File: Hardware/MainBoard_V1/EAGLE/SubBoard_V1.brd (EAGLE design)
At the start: 30 x 50 mm, 17 parts, among them J1 1X2-3.5MM, U1 MAX31855K

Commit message: Layout optimization
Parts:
- moved J4 8.00 mm to (20.0, 6.00)
- moved J5 8.00 mm to (20.0, 14.0)
- moved J6 8.00 mm to (20.0, 24.0)
- moved J8 8.00 mm to (20.0, 35.0)
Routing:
- net D8: track 9.89 -> 17.9 mm
- net A0: track 13.6 -> 5.55 mm
- net A7: track 15.4 -> 10.0 mm
- net A3: track 15.8 -> 10.7 mm
- net A6: track 15.6 -> 10.6 mm
- net A2: track 16.1 -> 11.8 mm
- net A1: track 16.3 -> 12.8 mm
- net 5V: track 64.7 -> 66.1 mm

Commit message: SubBoard exports
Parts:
- added C2: 10uF, rcl:C0805
- added D1, D2: (no value), adafruit:SOD-523
- added R1, R2: 10k, rcl:R0402
- C1: value (none) -> 0.01uF
- J5: device SparkFun-Connectors:JST-2-PTH-NS -> SparkFun-Connectors:JST-2-PTH
- moved J7 8.06 mm to (28.0, 43.0), turned to 180 degrees
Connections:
- new net N$4: D1.A, R1.1, U1.5
- new net N$6: D2.A, R2.1, U1.6
- net 3V3: now also C2.1, R1.2, R2.2, U1.4
- net 5V: no longer U1.4
- net D5: now also D2.K; no longer U1.6
- net D6: now also D1.K; no longer U1.5
- net GND: now also C2.2
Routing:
- net 3V3: track 0.00 -> 62.1 mm, vias 0 -> 2
- net N$4: track 0.00 -> 35.2 mm
- net D6: track 34.5 -> 2.04 mm
- net N$6: track 0.00 -> 31.8 mm
- net D5: track 33.7 -> 2.28 mm
- net D1: track 25.2 -> 21.9 mm
- net 5V: track 66.1 -> 63.1 mm, vias 1 -> 0
- net D0: track 24.2 -> 25.5 mm
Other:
- outline, holes or cut-outs redrawn
- board text added: "+ T R G"
- board text removed: "G R T +"

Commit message: Switch pullups added
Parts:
- added R3, R4: 10K, rcl:R0402
- R1, R2: value 10k -> 10K
- moved J7 3.00 mm to (28.0, 46.0)
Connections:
- net 5V: now also R3.2, R4.2
- net A6: now also R3.1
- net A7: now also R4.1
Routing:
- net 5V: track 63.1 -> 73.4 mm
- net D1: track 21.9 -> 24.1 mm
- net A6: track 10.6 -> 12.4 mm
- net A7: track 10.0 -> 11.9 mm
- net D0: track 25.5 -> 27.0 mm

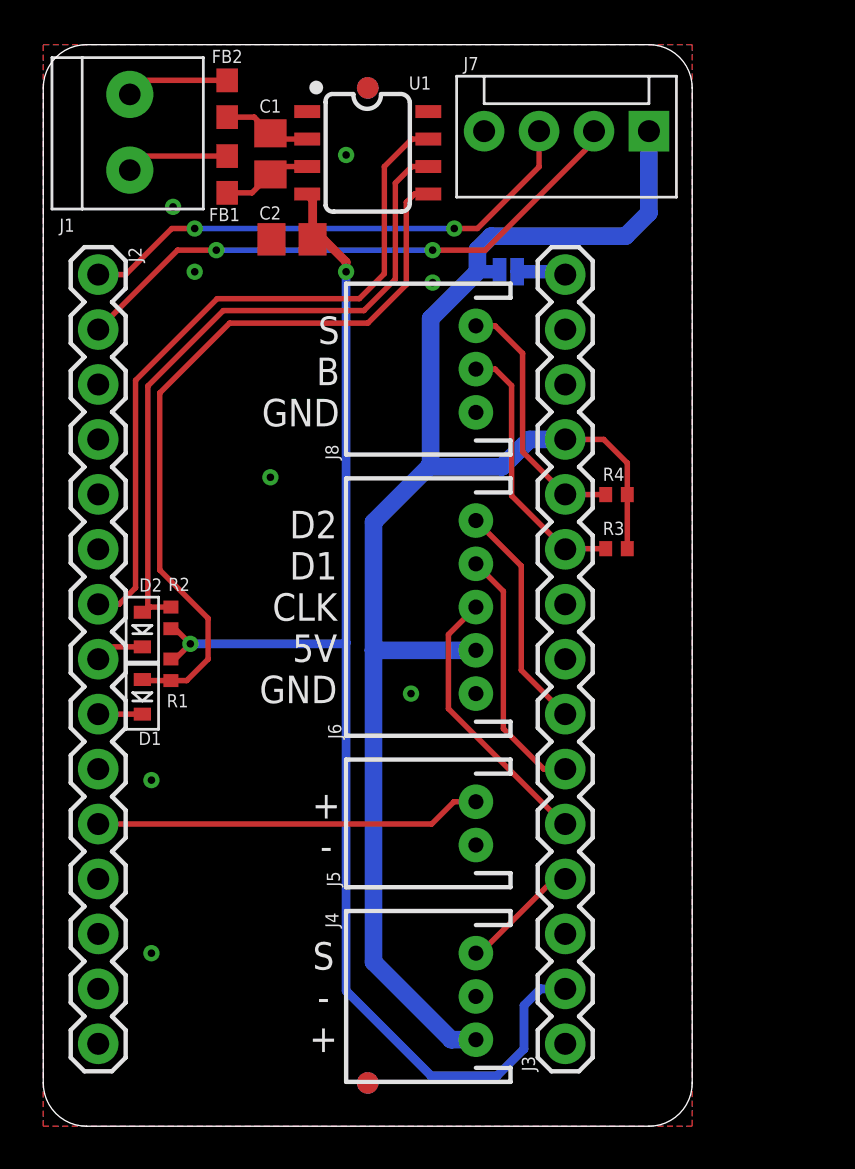
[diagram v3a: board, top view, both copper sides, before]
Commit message: Layout change
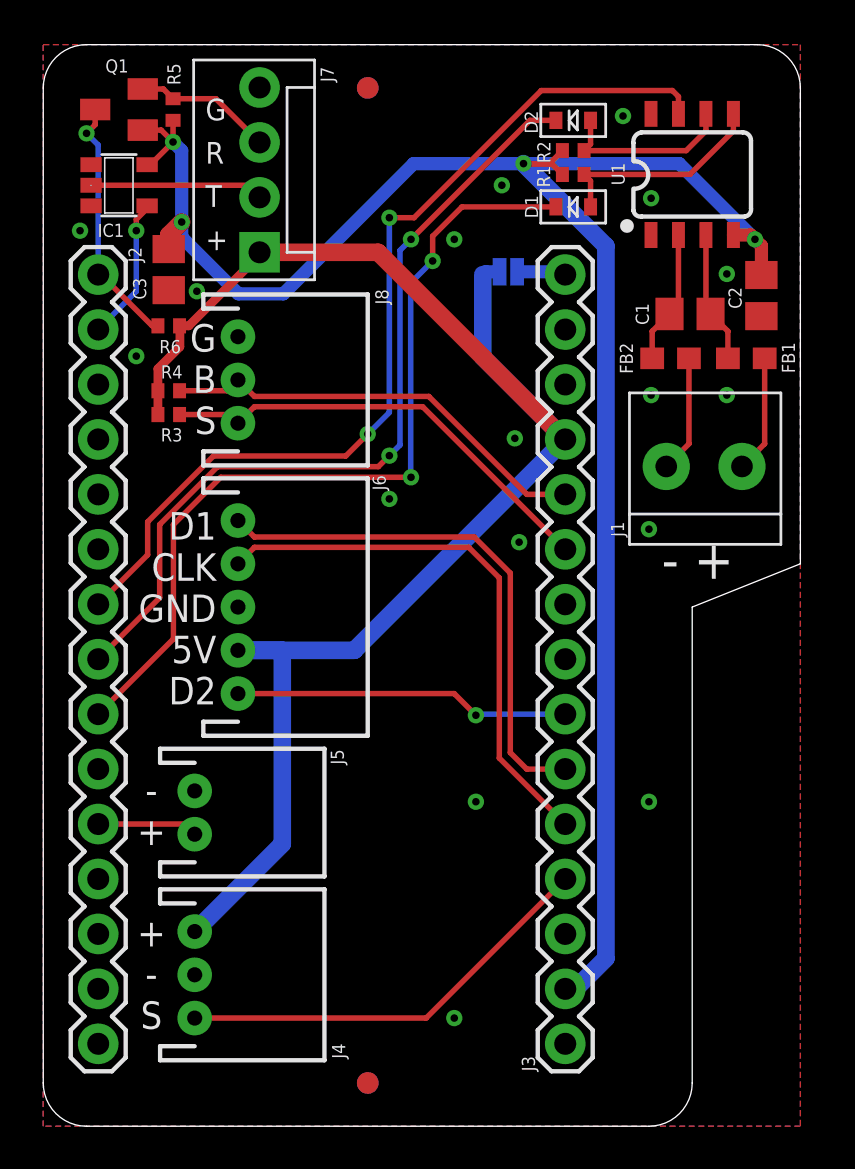
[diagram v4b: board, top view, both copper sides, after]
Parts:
- added C3: 10uF, rcl:C0805
- added IC1: (no value), 74xx-little-de:SOT23-5
- added Q1: (no value), adafruit:SOT23
- added R5, R6: 10K, rcl:R0402
- moved D2 30.8 mm to (24.5, 46.5), turned to 90 degrees
- moved J1 30.7 mm to (30.5, 30.5), turned to 0 degrees
- moved D1 30.2 mm to (24.5, 42.5), turned to 90 degrees
- moved R1 29.5 mm to (24.5, 44.0), turned to 180 degrees
- moved R2 28.5 mm to (24.5, 45.1), turned to 180 degrees
- moved FB1 25.5 mm to (32.5, 35.5), turned to 180 degrees
- moved FB2 23.8 mm to (29.0, 35.5), turned to 180 degrees
- moved C2 21.9 mm to (33.2, 38.4), turned to 270 degrees
- moved R3 21.6 mm to (5.80, 32.9), turned to 180 degrees
- moved R4 21.2 mm to (5.80, 34.0), turned to 180 degrees
- moved C1 20.8 mm to (29.9, 37.5), turned to 0 degrees
- moved J7 18.9 mm to (10.0, 40.4), turned to 90 degrees
- moved U1 15.0 mm to (30.0, 44.0), turned to 0 degrees
- moved J4 13.0 mm to (7.00, 7.00), turned to 270 degrees
- moved J5 13.0 mm to (7.00, 14.5), turned to 270 degrees
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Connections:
- new net RX: J7.3, Q1.2, R5.1
- new net TX: IC1.2, J7.2
- net 3V3: now also C3.1, IC1.5, Q1.1, R5.2
- net 5V: now also J6.4, R6.2; no longer J6.2
- net A1: now also J6.2; no longer J6.3
- net A2: now also J6.1; no longer J6.4
- net A6: now also J8.3; no longer J8.2
- net A7: now also J8.2; no longer J8.3
- net D0: now also IC1.4; no longer J7.2
- net D1: now also Q1.3, R6.1; no longer J7.3
- net GND: now also C3.2, IC1.3, J6.3; no longer J6.1
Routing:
- net D6: track 2.04 -> 39.9 mm, vias 0 -> 2
- net D5: track 2.28 -> 38.7 mm, vias 0 -> 2
- net 3V3: track 62.1 -> 89.5 mm, vias 2 -> 4
- net N$4: track 35.2 -> 10.2 mm
- net N$6: track 31.8 -> 8.32 mm
- net D0: track 27.0 -> 6.66 mm, vias 2 -> 1
- net A0: track 5.55 -> 19.8 mm
- net D8: track 17.9 -> 4.65 mm
- net A2: track 11.8 -> 24.8 mm
- net A1: track 12.8 -> 25.6 mm
- net D1: track 24.1 -> 11.8 mm, vias 2 -> 1
- net D4: track 32.7 -> 43.7 mm, vias 0 -> 2
- net A6: track 12.4 -> 21.0 mm
- net A7: track 11.9 -> 20.2 mm
- net TX: track 0.00 -> 8.02 mm
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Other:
- board size 30 x 50 mm -> 35 x 50 mm
- board text added: "+ - S"
- board text added: "- +"
- board text added: "D1 CLK GND 5V D2"
- board text added: "G B S"
- board text added: "G R T +"
- board text removed: "+ -"
- board text removed: "+ T R G"
- board text removed: "D2 D1 CLK 5V GND"
- board text removed: "S - +"
- board text removed: "S B GND"
- board text removed: "T- T+"

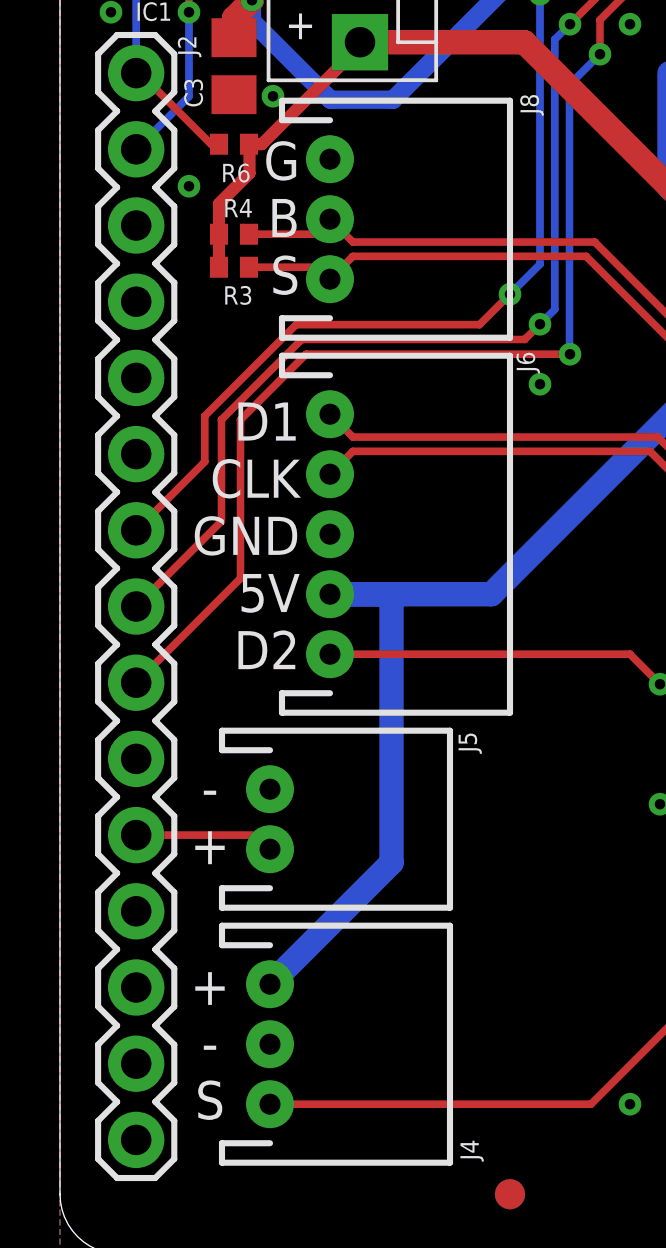
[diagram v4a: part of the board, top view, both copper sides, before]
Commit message: Boiler SSR pin relocation
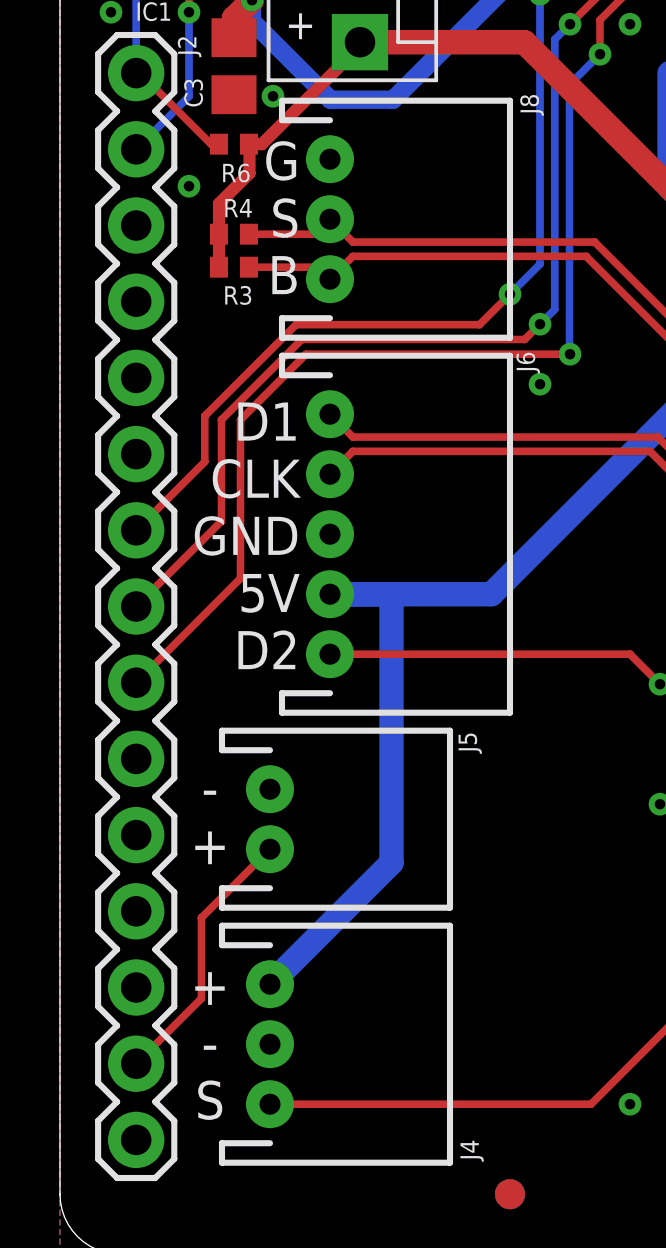
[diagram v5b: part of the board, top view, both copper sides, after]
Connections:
- net D11: now also J5.2
- net D8: no longer J5.2
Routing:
- net D11: track 0.00 -> 9.00 mm
- net D8: track 4.65 -> 0.00 mm
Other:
- board text added: "G S B"
- board text removed: "G B S"
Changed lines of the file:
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@@
 <drawing>
 <settings>
-<setting alwaysvectorfont="yes"/>
+<setting alwaysvectorfont="no"/>
 <setting verticaltext="up"/>
 </settings>
-<grid distance="1" unitdist="mm" unit="mm" style="lines" multiple="1" display="no" altdistance="0.1" altunitdist="mm" altunit="mm"/>
+<grid distance="50" unitdist="mil" unit="mil" style="lines" multiple="1" display="no" altdistance="5" altunitdist="mil" altunit="mil"/>
 <layers>
 <layer number="1" name="Top" color="4" fill="1" visible="yes" active="yes"/>
@@
 <text x="26.714" y="1.534" size="1.778" layer="26" rot="MR90">Gaggiuino</text>
 <text x="8" y="32" size="1.27" layer="25" align="bottom-right">G
-B
-S</text>
+S
+B</text>
 <text x="8" y="19.5" size="1.27" layer="25" align="bottom-right">D1
 CLK
@@
 <signal name="D11">
 <contactref element="J2" pad="14"/>
+<contactref element="J5" pad="2"/>
+<wire x1="2.54" y1="6.35" x2="4.714" y2="8.524" width="0.254" layer="1"/>
+<wire x1="4.714" y1="11.214" x2="7" y2="13.5" width="0.254" layer="1"/>
+<wire x1="4.714" y1="11.214" x2="4.714" y2="8.524" width="0.254" layer="1"/>
 </signal>
 <signal name="D10">
@@
 <signal name="D8">
 <contactref element="J2" pad="11"/>
-<contactref element="J5" pad="2"/>
-<wire x1="7" y1="13.5" x2="6.53" y2="13.97" width="0.254" layer="1"/>
-<wire x1="6.53" y1="13.97" x2="2.54" y2="13.97" width="0.254" layer="1"/>
 </signal>
 <signal name="D7">

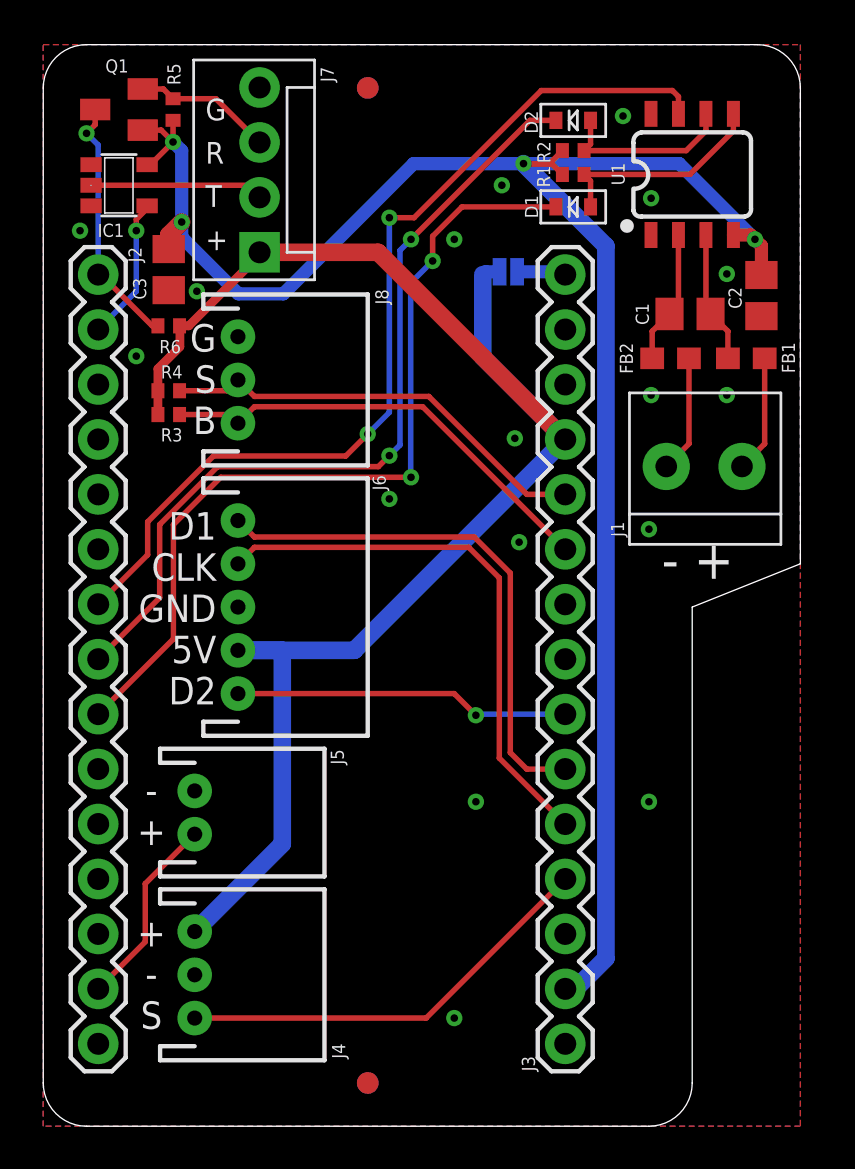
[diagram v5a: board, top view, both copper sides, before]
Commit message: Nextion full buffer IO
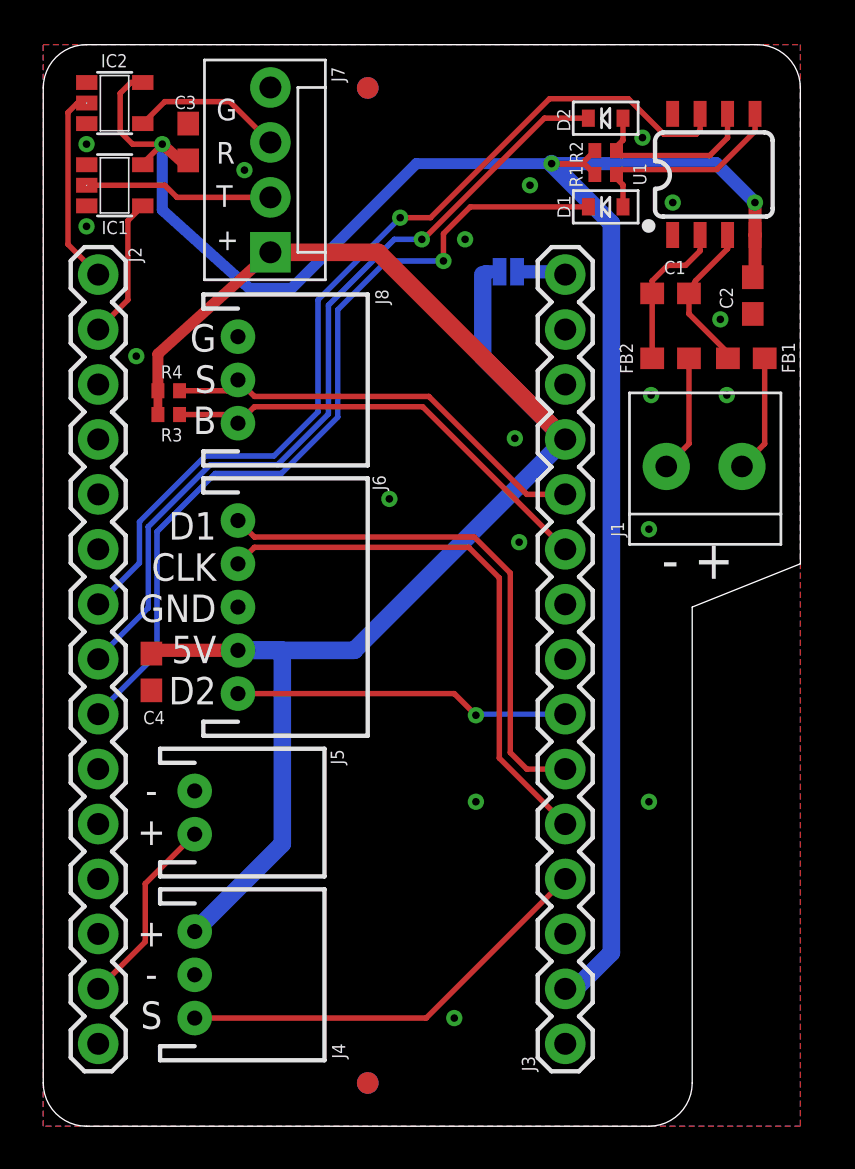
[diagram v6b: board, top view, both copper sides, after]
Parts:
- removed Q1: (no value), adafruit:SOT23
- removed R5, R6: 10K, rcl:R0402
- added C4: 10uF, rcl:C0603
- added IC2: (no value), 74xx-little-de:SOT23-5
- C1, C2, C3: device rcl:C0805 -> rcl:C0603
- moved C3 5.97 mm to (6.70, 45.5), turned to 90 degrees
- moved D2 1.50 mm to (26.0, 46.6)
- moved D1 1.50 mm to (26.0, 42.5)
- moved R1 1.50 mm to (26.0, 44.0)
- moved R2 1.50 mm to (26.0, 45.1)
- moved C1 1.31 mm to (29.0, 38.5)
- moved U1 1.00 mm to (31.0, 44.0)
- moved J7 0.50 mm to (10.5, 40.4)
- moved C2 0.40 mm to (32.8, 38.4)
- moved IC1 0.20 mm to (3.30, 43.5)
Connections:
- net 3V3: now also IC2.5; no longer Q1.1, R5.2
- net 5V: now also C4.1; no longer R6.2
- net D1: now also IC2.2; no longer Q1.3, R6.1
- net GND: now also C4.2, IC2.3
- net RX: now also IC2.4; no longer Q1.2, R5.1
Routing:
- net 5V: track 73.3 -> 77.0 mm
- net D1: track 11.8 -> 9.12 mm, vias 1 -> 0
- net 3V3: track 89.5 -> 91.5 mm, vias 4 -> 3
- net N$5: track 6.12 -> 7.13 mm
- net N$3: track 6.20 -> 7.10 mm
- net TX: track 8.02 -> 8.72 mm
- net RX: track 6.42 -> 7.11 mm
- net D4: track 43.7 -> 43.2 mm, vias 2 -> 1
- net D6: track 39.9 -> 39.4 mm, vias 2 -> 1
- net D5: track 38.7 -> 38.2 mm, vias 2 -> 1
- net D0: track 6.66 -> 6.57 mm, vias 1 -> 0

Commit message: Connector spacing fixed
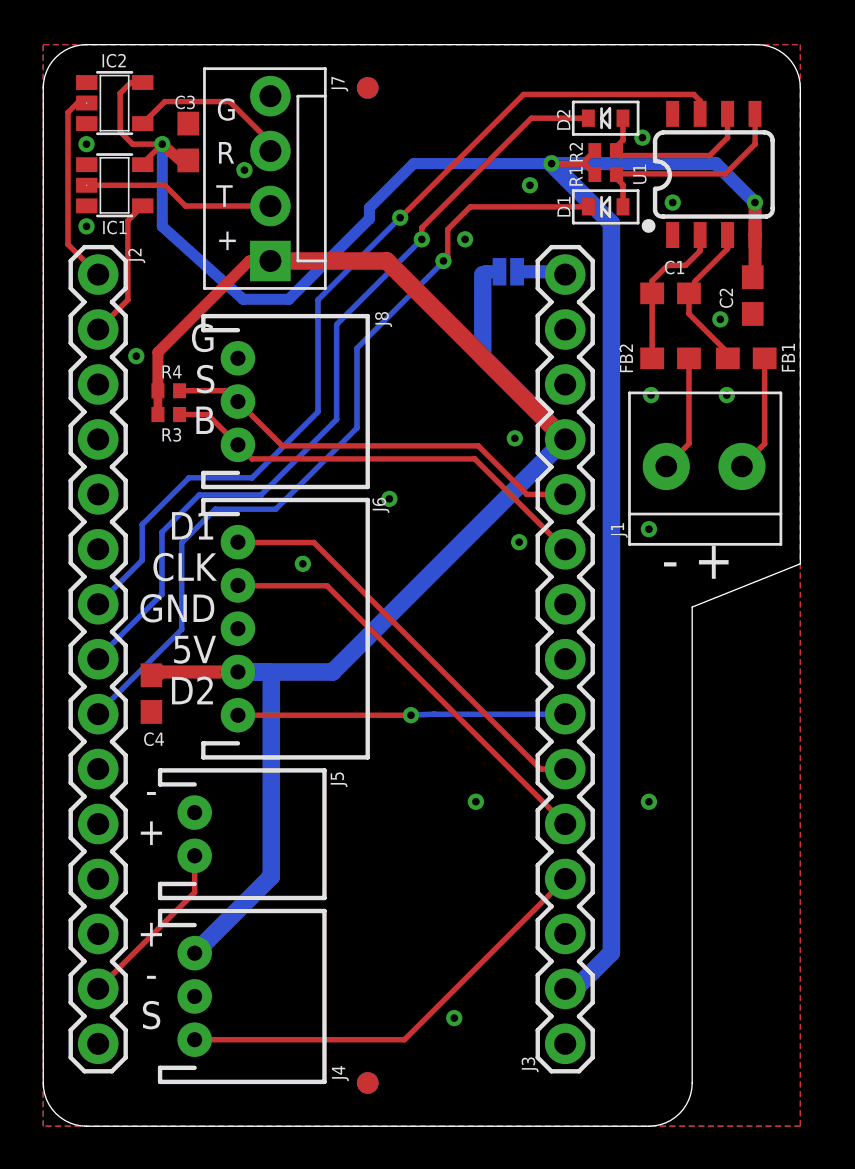
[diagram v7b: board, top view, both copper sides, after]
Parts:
- moved C4 1.00 mm to (5.00, 20.0)
- moved J4 1.00 mm to (7.00, 6.00)
- moved J5 1.00 mm to (7.00, 13.5)
- moved J6 1.00 mm to (9.00, 23.0)
- moved J8 1.00 mm to (9.00, 33.5)
- moved J7 0.40 mm to (10.5, 40.0)
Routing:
- net A1: track 25.6 -> 19.7 mm
- net A2: track 24.8 -> 19.5 mm
- net D6: track 39.4 -> 37.7 mm
- net 3V3: track 91.5 -> 92.6 mm
- net D11: track 9.00 -> 8.00 mm
- net D4: track 43.2 -> 42.3 mm
- net A6: track 21.0 -> 20.4 mm
- net D5: track 38.2 -> 37.6 mm

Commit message: Switch reassignment
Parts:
- removed R4: 10K, rcl:R0402
- added C5: 0.1uF, rcl:C0603
- moved R3 10.0 mm to (6.70, 42.9), turned to 270 degrees
- moved C2 8.10 mm to (33.0, 46.5), turned to 90 degrees
- moved U1 2.24 mm to (29.0, 45.0)
- moved D2 2.00 mm to (24.0, 46.5)
- moved R2 2.00 mm to (24.0, 45.0)
- moved D1 2.00 mm to (24.0, 42.5)
- moved FB1 2.00 mm to (32.5, 37.5)
- moved FB2 2.00 mm to (29.0, 37.5)
- moved J1 2.00 mm to (30.5, 32.5)
- moved R1 2.00 mm to (24.0, 44.0)
- moved C1 1.00 mm to (29.0, 39.5)
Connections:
- net 3V3: now also C5.1, R3.1
- net 5V: no longer R3.2, R4.2
- net A6: no longer J8.3, R3.1
- net A7: no longer J8.2, R4.1
- net D7: now also J8.2
- net D8: now also J8.3
- net GND: now also C5.2
- net TX: now also R3.2
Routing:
- net D7: track 0.00 -> 39.8 mm, vias 0 -> 2
- net D8: track 0.00 -> 38.1 mm, vias 0 -> 2
- net A6: track 20.4 -> 0.00 mm
- net A7: track 19.8 -> 0.00 mm
- net 5V: track 76.6 -> 66.8 mm
- net N$3: track 7.10 -> 4.79 mm
- net 3V3: track 92.6 -> 94.8 mm
- net D6: track 37.7 -> 35.9 mm
- net N$5: track 7.13 -> 5.57 mm
- net N$4: track 10.1 -> 11.1 mm
- net N$6: track 8.32 -> 9.23 mm
- net D5: track 37.6 -> 37.1 mm
